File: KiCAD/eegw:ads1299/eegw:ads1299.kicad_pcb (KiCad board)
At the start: 2 copper layers, 88 x 116.5 mm, 122 parts, among them J1 ESP32-L, J10 ESP32-R2, J2 ESP32-L3, J3 ESP32-L2, J4 ESP32_Left, J5 ESP32_Right, J6 ESP32-R, J8 Conn_01x10, J9 gpioADS, U1 ADS1299IPAG, U2 INA128U, U3 INA128U, U4 INA128U, U5 INA128U, U6 INA128U, U7 INA128U, U8 INA128U, U9 INA128U

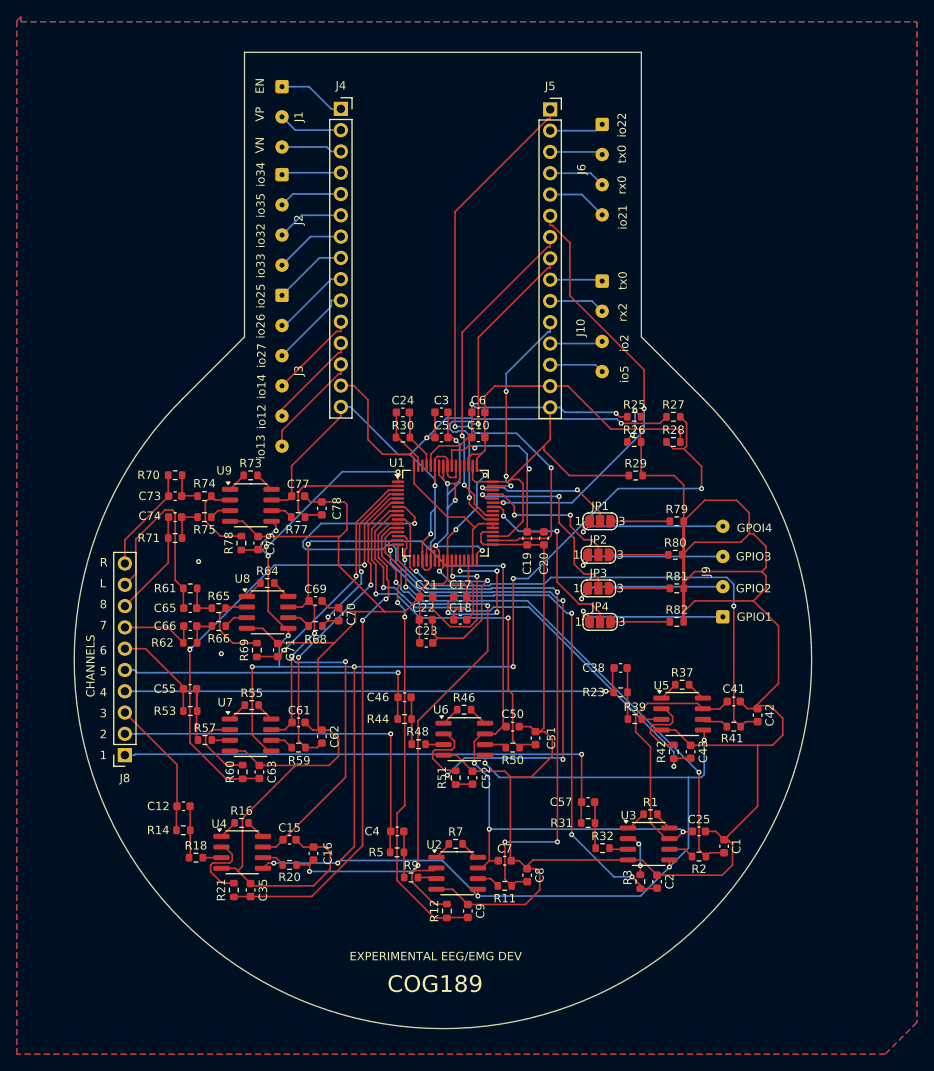
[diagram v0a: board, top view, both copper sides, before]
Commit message: updated kicad renumbered
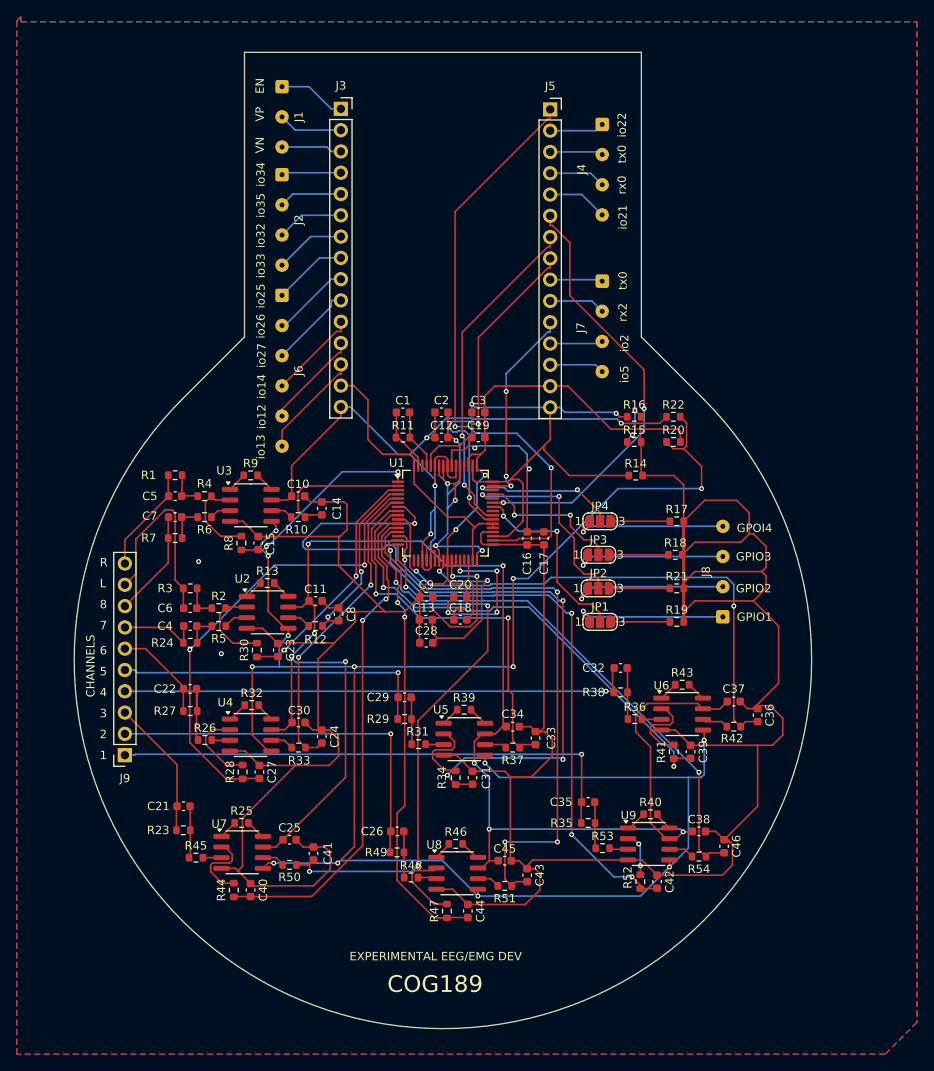
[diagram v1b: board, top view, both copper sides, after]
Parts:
- renumbered C24 to C1, C77 to C10, C69 to C11, C5 to C12, C22 to C13, C78 to C14, C79 to C15, C19 to C16, C20 to C17, C10 to C19, C3 to C2, C17 to C20, C12 to C21, C55 to C22, C71 to C23, C62 to C24, C15 to C25, C4 to C26, C63 to C27, C23 to C28, C46 to C29, C6 to C3, C61 to C30, C52 to C31, C38 to C32, C51 to C33, C50 to C34, C57 to C35, C42 to C36, C41 to C37, C25 to C38, C43 to C39, C66 to C4, C35 to C40, C16 to C41, C2 to C42, C8 to C43, C9 to C44, C7 to C45, C1 to C46, C73 to C5, C65 to C6, C74 to C7, C70 to C8, C21 to C9, J4 to J3, J6 to J4, J3 to J6, J10 to J7, J9 to J8, J8 to J9, JP4 to JP1, JP3 to JP2, JP2 to JP3, JP1 to JP4, R70 to R1, R77 to R10, R30 to R11, R68 to R12, R64 to R13, R29 to R14, R26 to R15, R25 to R16, R79 to R17, R80 to R18, R82 to R19, R65 to R2, R28 to R20, R81 to R21, R27 to R22, R14 to R23, R62 to R24, R16 to R25, R57 to R26, R53 to R27, R60 to R28, R44 to R29, R61 to R3, R69 to R30, R48 to R31, R55 to R32, R59 to R33, R51 to R34, R31 to R35, R39 to R36, R50 to R37, R23 to R38, R46 to R39, R74 to R4, R1 to R40, R42 to R41, R41 to R42, R37 to R43, R21 to R44, R18 to R45, R7 to R46, R12 to R47, R9 to R48, R5 to R49, R66 to R5, R20 to R50, R11 to R51, R3 to R52, R32 to R53, R2 to R54, R75 to R6, R71 to R7, R78 to R8, R73 to R9, U8 to U2, U9 to U3, U7 to U4, U6 to U5, U5 to U6, U4 to U7, U2 to U8, U3 to U9
